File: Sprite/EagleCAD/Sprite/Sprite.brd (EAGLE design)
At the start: 35 x 35 mm, 27 parts, among them Q1 26MHz, U1 CC430F5137, U2 HMC5883LSMD, U3 ITG-3200

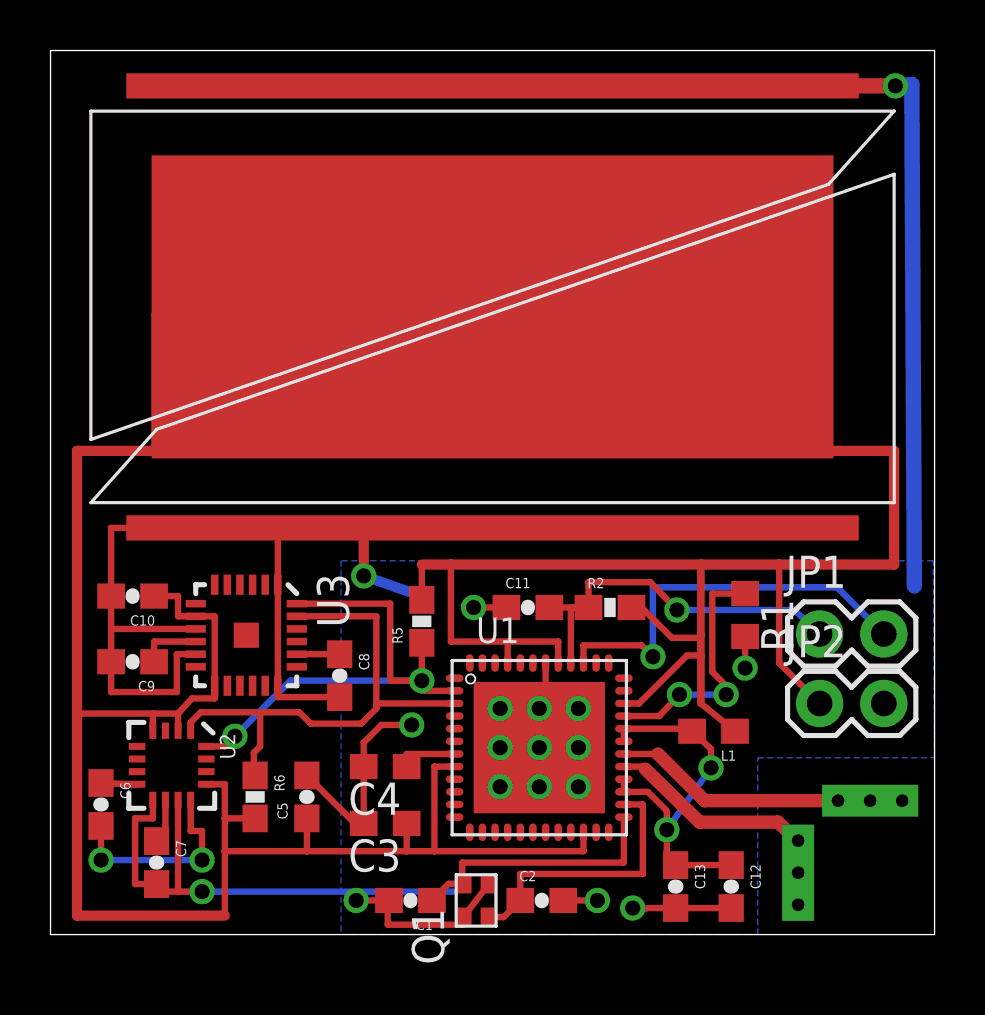
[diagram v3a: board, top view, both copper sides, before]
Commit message: XTAL and Solar Cell fixes
Fixed alignment of crystal and moved ground pads on TASC cells further
apart
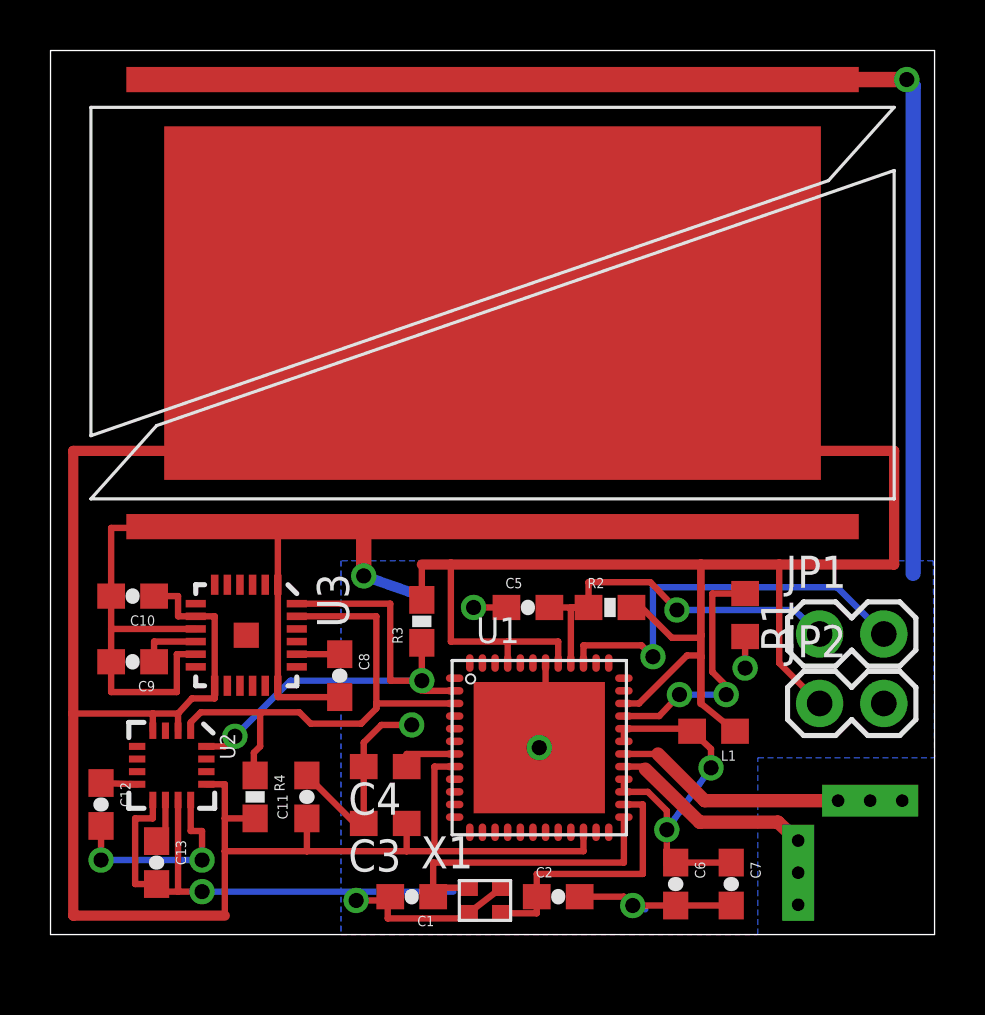
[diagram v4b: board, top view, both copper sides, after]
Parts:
- removed Q1: 26MHz, ABM11_JAA:ABM11_CERAMIC-SMD-CRYSTAL
- removed S1: TASC, TASC:TASC
- added U$3: TASC, TASC:TASC
- added X1: ABM11_CERAMIC_SMD_CRYSTALABM11, ABM11:ABM11_CERAMIC-SMD-CRYSTAL
- C1, C2: value 27 pF -> 27pF
- C11: value 2.2 nF -> 100nF
- C12: value 100 Nf -> 220nF
- C13: value 10 Nf -> 4.7uF
- C3, C4: value 470 nF -> 470nF
- C5: value .1uF -> 2.2nF
- C6: value .22uF -> 100nF
- C7: value 4.7uF -> 10nF
- C9: value 0.1uF -> 100nF
- moved C12 25.2 mm to (2.00, 5.15)
- moved C6 23.0 mm to (24.8, 2.00)
- moved C7 22.8 mm to (26.9, 2.00)
- moved C13 20.6 mm to (4.20, 2.85)
- moved C11 11.5 mm to (10.2, 5.45), turned to 90 degrees
- moved C5 11.5 mm to (18.9, 12.9), turned to 0 degrees
- moved C2 0.67 mm to (20.1, 1.50)
- moved C1 0.16 mm to (14.3, 1.50)
- renumbered R5 to R3, R6 to R4
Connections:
- net GND: now also C11.2, C5.1, C6.2, U$3.MINUS1, U$3.MINUS2, X1.P2, X1.P4; no longer C11.1, C12.2, C5.2, Q1.P$2, Q1.P$4, S1.MINUS1, S1.MINUS2
- net N$1: now also X1.P3; no longer Q1.P$3
- net N$2: now also X1.P1; no longer Q1.P$1
- net N$5: now also C12.1; no longer C6.1
- net N$6: now also C12.2; no longer C6.2
- net N$7: now also C13.1; no longer C7.1
- net RST: now also C5.2; no longer C11.2
- net VCC: now also C11.1, U$3.PLUS; no longer C5.1, S1.PLUS
- net VCCRF: now also C6.1, C7.1; no longer C12.1, C13.1
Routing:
- net VCC: track 145.2 -> 151.8 mm
- net GND: track 130.9 -> 132.9 mm, vias 18 -> 9
- net N$2: track 10.6 -> 12.4 mm

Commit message: Added LED for debugging purposes, fixed crystal layout
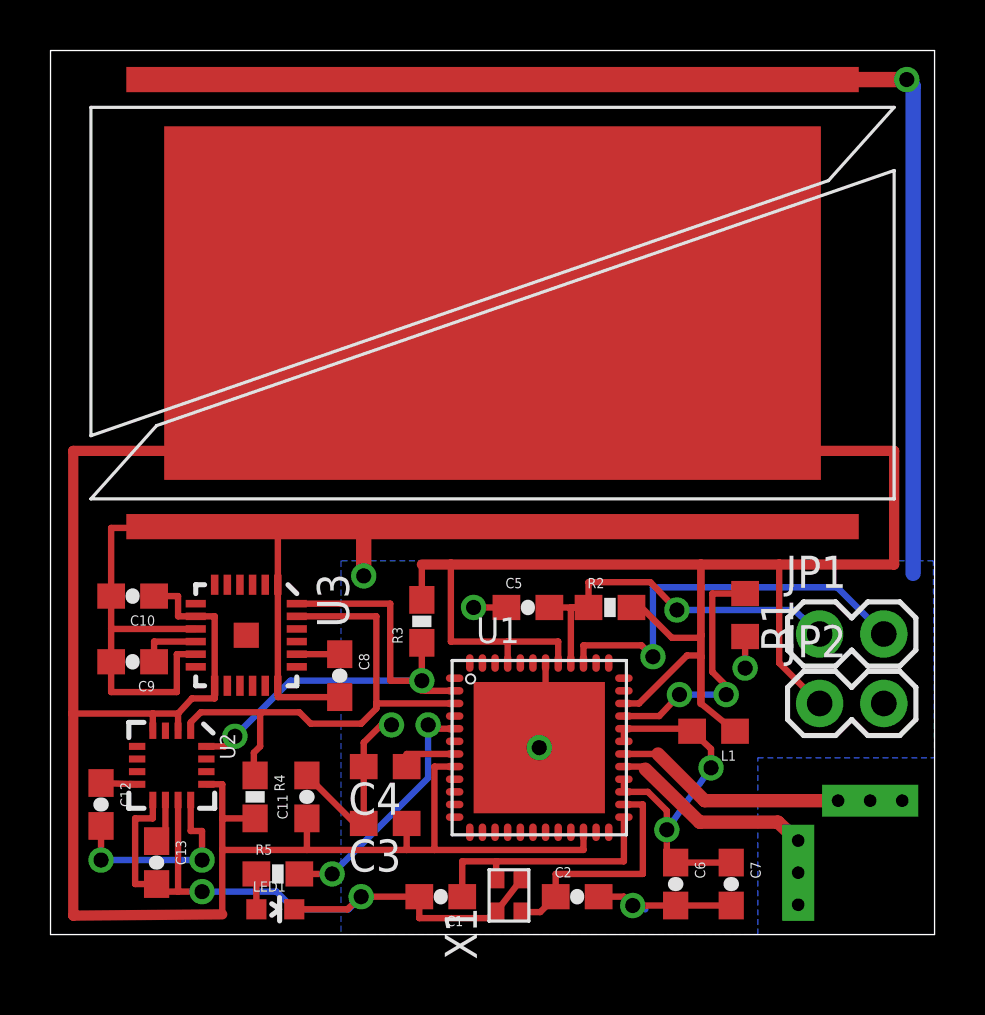
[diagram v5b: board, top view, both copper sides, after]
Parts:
- added LED1: (no value), SparkFun:LED-0603
- added R5: 270R, SparkFun:0603-RES
- moved C1 1.15 mm to (15.4, 1.50)
- moved X1 0.97 mm to (18.1, 1.55), turned to 90 degrees
- moved C2 0.75 mm to (20.9, 1.50)
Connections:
- new net N$10: R5.2, U1.5
- new net N$11: LED1.A, R5.1
- net GND: now also LED1.C, X1.P$2, X1.P$4; no longer X1.P2, X1.P4
- net N$1: now also X1.P$3; no longer X1.P3
- net N$2: now also X1.P$1; no longer X1.P1
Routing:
- net N$10: track 0.00 -> 9.89 mm, vias 0 -> 2
- net GND: track 132.9 -> 130.1 mm
- net N$2: track 12.4 -> 10.2 mm
- net N$11: track 0.00 -> 1.40 mm
- net N$1: track 10.6 -> 9.44 mm

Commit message: Some cleanup, updated BOM
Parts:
- X1: value ABM11_CERAMIC_SMD_CRYSTALABM11 -> 26 MHz
- renumbered U$1 to ANT-N, U$2 to ANT-P, U$3 to S1
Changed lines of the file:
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@@
 <element name="JP1" library="SparkFun" package="1X02" value="" x="30.45" y="11.9"/>
 <element name="JP2" library="SparkFun" package="1X02" value="" x="30.45" y="9.15"/>
-<element name="U$1" library="SpriteAntenna" package="ANTENNA" value="ANTENNA" x="32.45" y="5.3" rot="R180"/>
-<element name="U$2" library="SpriteAntenna" package="ANTENNA" value="ANTENNA" x="29.6" y="2.45" rot="R90"/>
+<element name="ANT-N" library="SpriteAntenna" package="ANTENNA" value="ANTENNA" x="32.45" y="5.3" rot="R180"/>
+<element name="ANT-P" library="SpriteAntenna" package="ANTENNA" value="ANTENNA" x="29.6" y="2.45" rot="R90"/>
 <element name="R2" library="SparkFun" package="0603-RES" value="47K" x="22.15" y="12.95"/>
 <element name="C5" library="SparkFun" package="0603-CAP" value="2.2nF" x="18.9" y="12.95"/>
@@
 <element name="C7" library="SparkFun" package="0603-CAP" value="10nF" x="26.95" y="2" rot="R270"/>
 <element name="C6" library="SparkFun" package="0603-CAP" value="100nF" x="24.75" y="2" rot="R270"/>
-<element name="U$3" library="TASC" package="TASC" value="TASC" x="1.6" y="17.25"/>
+<element name="S1" library="TASC" package="TASC" value="TASC" x="1.6" y="17.25"/>
 <element name="LED1" library="SparkFun" package="LED-0603" value="" x="8.9" y="1" rot="R270"/>
 <element name="R5" library="SparkFun" package="0603-RES" value="270R" x="9" y="2.4"/>
-<element name="X1" library="ABM11" package="ABM11_CERAMIC-SMD-CRYSTAL" value="ABM11_CERAMIC_SMD_CRYSTALABM11" x="18.15" y="1.55" rot="R90"/>
+<element name="X1" library="ABM11" package="ABM11_CERAMIC-SMD-CRYSTAL" value="26 MHz" x="18.15" y="1.55" rot="R90"/>
 </elements>
 <signals>
@@
 <wire x1="24.6" y1="11.75" x2="25.65" y2="11.75" width="0.254" layer="1"/>
 <wire x1="25.65" y1="11.75" x2="25.75" y2="11.85" width="0.254" layer="1"/>
-<contactref element="U$3" pad="PLUS"/>
+<contactref element="S1" pad="PLUS"/>
 <wire x1="0.9" y1="19.15" x2="17.55" y2="19.15" width="0.4064" layer="1"/>
 <wire x1="17.55" y1="19.15" x2="17.55" y2="24.85" width="0.4064" layer="1"/>
@@
 <wire x1="21.7" y1="1.5" x2="22.7" y2="1.5" width="0.254" layer="1"/>
 <wire x1="22.7" y1="1.5" x2="23.05" y2="1.15" width="0.254" layer="1"/>
-<contactref element="U$3" pad="MINUS1"/>
-<contactref element="U$3" pad="MINUS2"/>
+<contactref element="S1" pad="MINUS1"/>
+<contactref element="S1" pad="MINUS2"/>
 <wire x1="17.5" y1="16.15" x2="12.4" y2="16.15" width="0.4064" layer="1"/>
 <wire x1="12.4" y1="16.15" x2="12.4" y2="16.1" width="0.4064" layer="1"/>
@@
 <signal name="RFN">
 <contactref element="U1" pad="30"/>
-<contactref element="U$1" pad="IN1"/>
-<contactref element="U$1" pad="IN3"/>
-<contactref element="U$1" pad="IN2"/>
+<contactref element="ANT-N" pad="IN1"/>
+<contactref element="ANT-N" pad="IN3"/>
+<contactref element="ANT-N" pad="IN2"/>
 <wire x1="32.45" y1="5.3" x2="33.72" y2="5.3" width="0.53" layer="1"/>
 <wire x1="31.18" y1="5.3" x2="32.45" y2="5.3" width="0.53" layer="1"/>
@@
 <signal name="RFP">
 <contactref element="U1" pad="29"/>
-<contactref element="U$2" pad="IN1"/>
-<contactref element="U$2" pad="IN3"/>
-<contactref element="U$2" pad="IN2"/>
+<contactref element="ANT-P" pad="IN1"/>
+<contactref element="ANT-P" pad="IN3"/>
+<contactref element="ANT-P" pad="IN2"/>
 <wire x1="29.6" y1="2.45" x2="29.6" y2="3.7" width="0.53" layer="1"/>
 <wire x1="29.6" y1="3.7" x2="29.6" y2="3.72" width="0.254" layer="1"/>
@@
 </signal>
 </signals>
-<errors>
-</errors>
 </board>
 </drawing>
